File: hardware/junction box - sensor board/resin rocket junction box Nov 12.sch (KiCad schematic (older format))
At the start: 34 parts, among them P1 M3021-000005-2K5PG, P2 M3021-000005-2K5PG, T1 MCP9600, T2 MCP9600

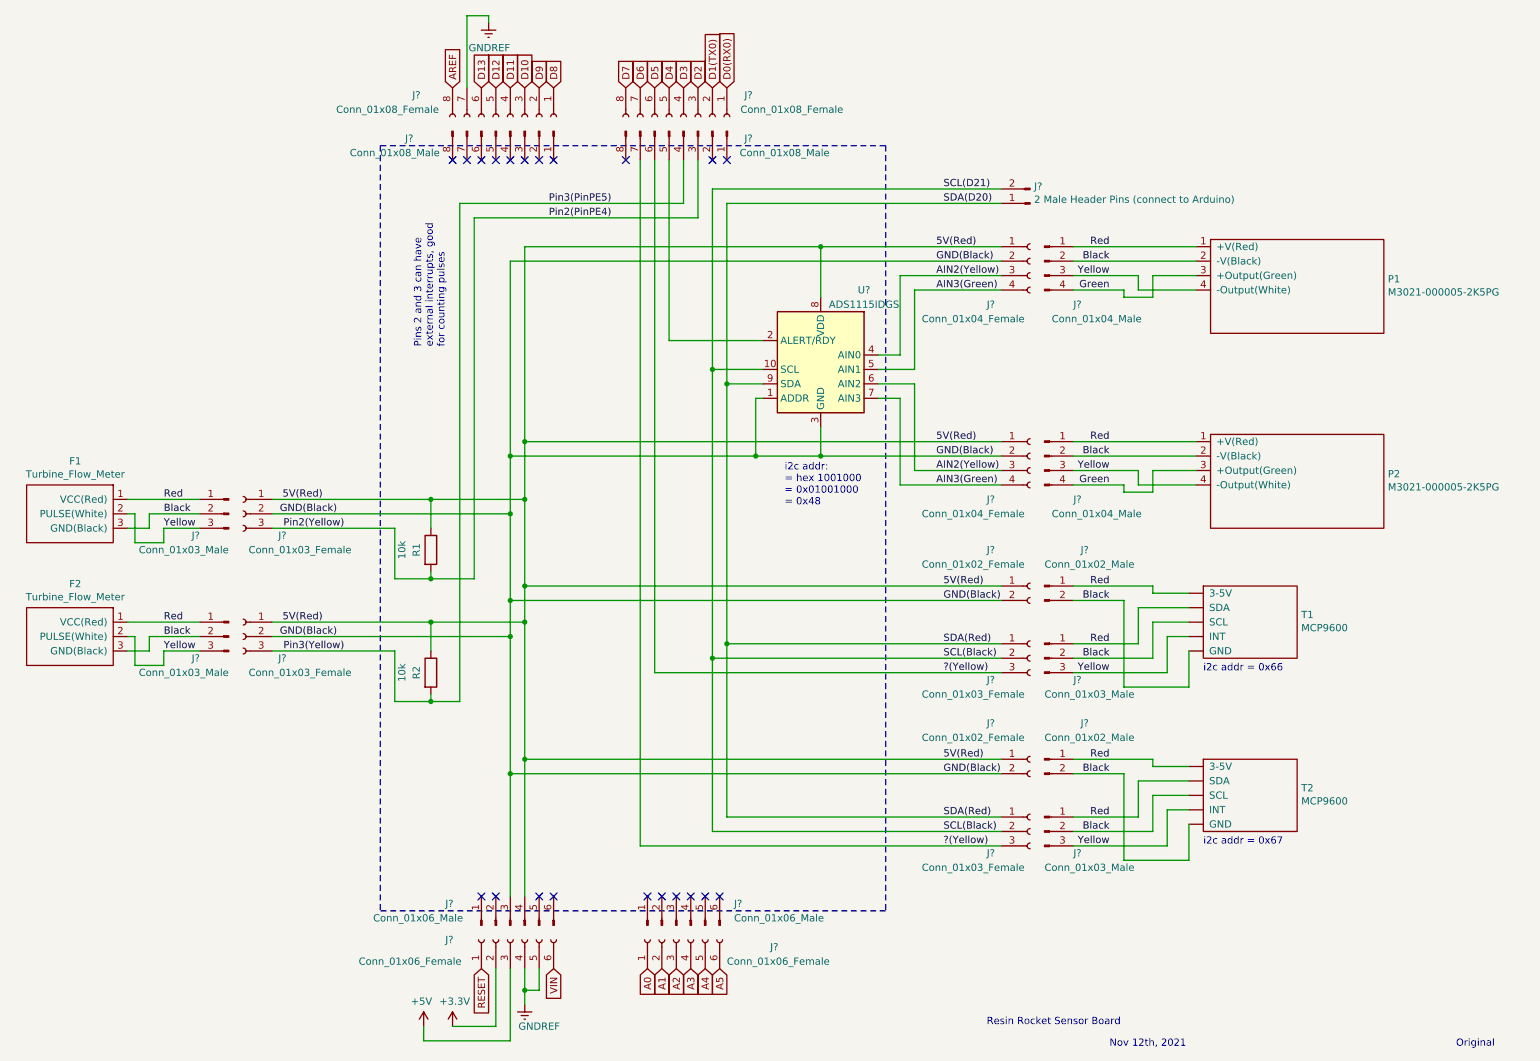
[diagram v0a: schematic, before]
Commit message: Updated all 3 schematics on Nov. 13th, 2021
Ground Station now includes buzzer, yellow LED, and voltage sensing circuit, to activate when key switch turns on high voltage lines (24V).

Split junction box boards into sensor board (connections to all sensors, ADCs, etc.) and high power board (controls the solenoids and igniter using 24V).
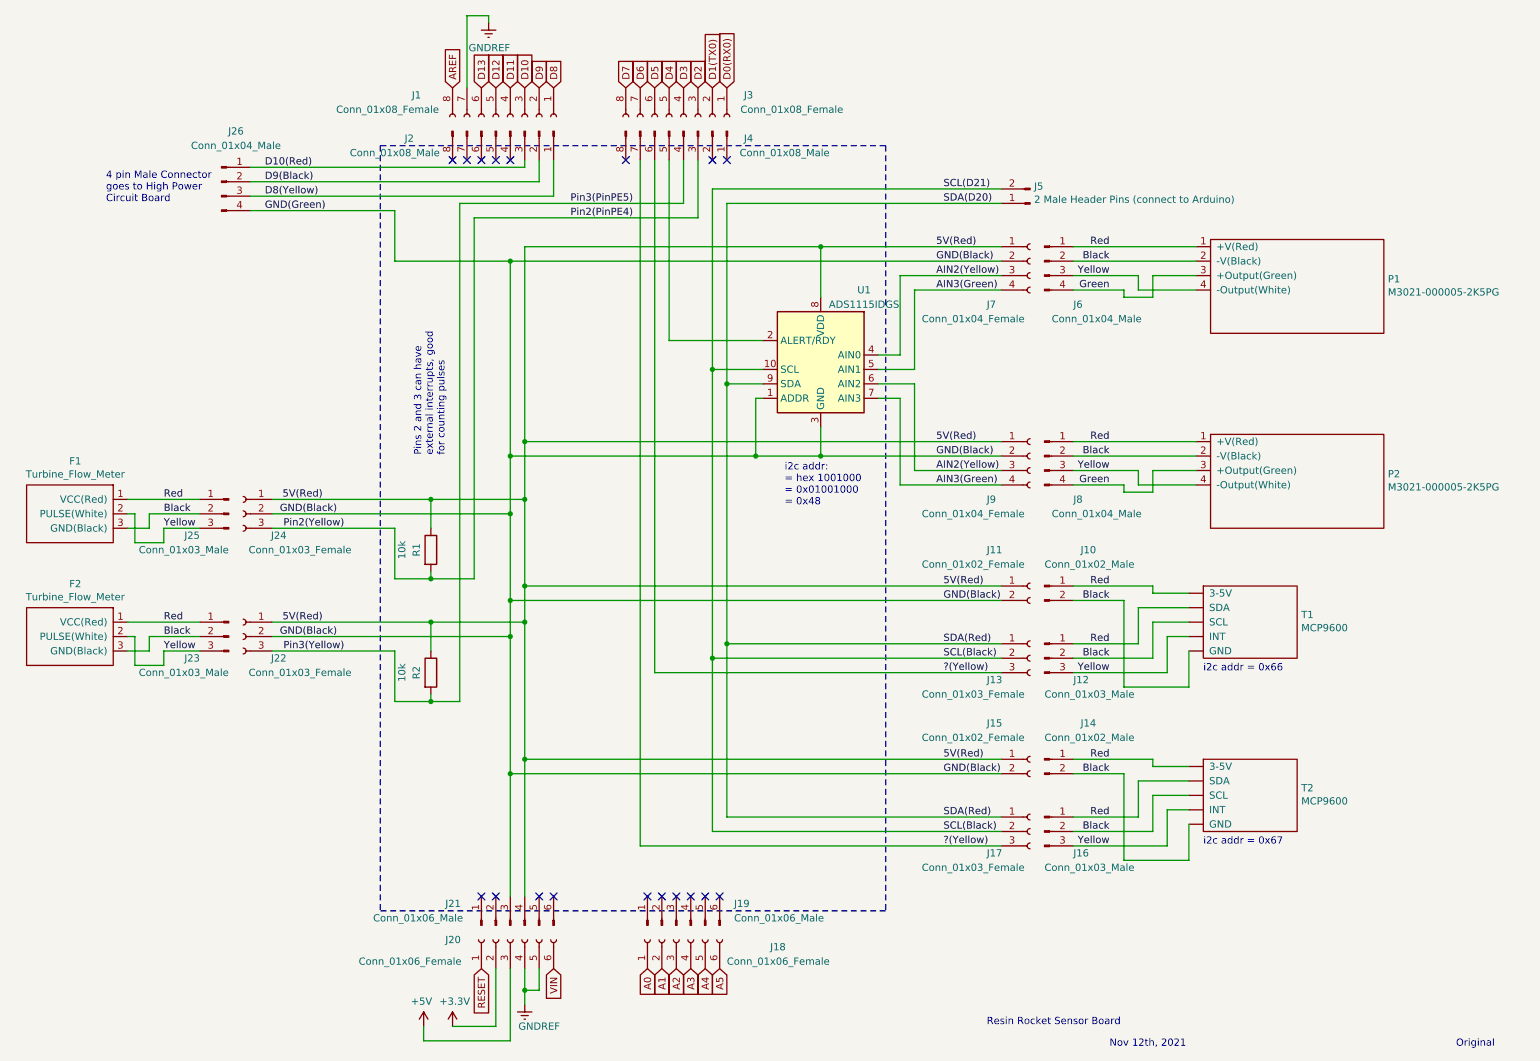
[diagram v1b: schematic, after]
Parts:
- added J26: Conn_01x04_Male, symbol Connector:Conn_01x04_Male
- gave numbers to parts that had none: 26
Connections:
- net GND(Black): now also J26.4 (Pin_4)
- net D8(Yellow): now reaches J2.1 (Pin_1)
- net D8(Yellow): now also J26.3 (Pin_3)
- net D9(Black): now reaches J2.2 (Pin_2)
- net D9(Black): now also J26.2 (Pin_2)
- net D10(Red): now reaches J2.3 (Pin_3)
- net D10(Red): now also J26.1 (Pin_1)
- no-connect marks 21 -> 18
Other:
- note added: "4 pin Male Connector\ngoes to High Power\nCircuit Board"
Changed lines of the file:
@@
 ?(Yellow)
 $Comp
-L Connector:Conn_01x02_Female J?
+L Connector:Conn_01x02_Female J11
 U 1 1 61A4BA22
 P 7650 4450
-F 0 "J?" H 7350 4700 50  0000 L CNN
+F 0 "J11" H 7350 4700 50  0000 L CNN
 F 1 "Conn_01x02_Female" H 6900 4600 50  0000 L CNN
 F 2 "" H 7650 4450 50  0001 C CNN
@@
 GND(Black)
 $Comp
-L Connector:Conn_01x08_Male J?
+L Connector:Conn_01x08_Male J4
 U 1 1 61A54FC3
 P 5250 1300
-F 0 "J?" V 5300 1750 50  0000 C CNN
+F 0 "J4" V 5300 1750 50  0000 C CNN
 F 1 "Conn_01x08_Male" V 5400 2000 50  0000 C CNN
 F 2 "" H 5250 1300 50  0001 C CNN
@@
 $EndComp
 $Comp
-L Connector:Conn_01x06_Male J?
+L Connector:Conn_01x06_Male J19
 U 1 1 61A572F0
 P 5200 6800
-F 0 "J?" V 5350 6400 50  0000 R CNN
+F 0 "J19" V 5350 6400 50  0000 R CNN
 F 1 "Conn_01x06_Male" V 5250 6400 50  0000 R CNN
 F 2 "" H 5200 6800 50  0001 C CNN
@@
 $EndComp
 $Comp
-L Connector:Conn_01x06_Male J?
+L Connector:Conn_01x06_Male J21
 U 1 1 61A58D90
 P 4050 6800
-F 0 "J?" V 4200 7250 50  0000 R CNN
+F 0 "J21" V 4200 7250 50  0000 R CNN
 F 1 "Conn_01x06_Male" V 4100 7750 50  0000 R CNN
 F 2 "" H 4050 6800 50  0001 C CNN
@@
 $EndComp
 $Comp
-L Connector:Conn_01x08_Male J?
+L Connector:Conn_01x08_Male J2
 U 1 1 61A5C83D
 P 4050 1300
-F 0 "J?" V 4100 600 50  0000 C CNN
+F 0 "J2" V 4100 600 50  0000 C CNN
 F 1 "Conn_01x08_Male" V 4200 500 50  0000 C CNN
 F 2 "" H 4050 1300 50  0001 C CNN
@@
 $EndComp
 $Comp
-L Connector:Conn_01x08_Female J?
+L Connector:Conn_01x08_Female J1
 U 1 1 61A6B10B
 P 4050 1200
-F 0 "J?" V 3900 550 50  0000 C CNN
+F 0 "J1" V 3900 550 50  0000 C CNN
 F 1 "Conn_01x08_Female" V 4000 350 50  0000 C CNN
 F 2 "" H 4050 1200 50  0001 C CNN
@@
 $EndComp
 $Comp
-L Connector:Conn_01x08_Female J?
+L Connector:Conn_01x08_Female J3
 U 1 1 61A6C27C
 P 5250 1200
-F 0 "J?" V 5100 1650 50  0000 C CNN
+F 0 "J3" V 5100 1650 50  0000 C CNN
 F 1 "Conn_01x08_Female" V 5200 1950 50  0000 C CNN
 F 2 "" H 5250 1200 50  0001 C CNN
@@
 $EndComp
 $Comp
-L Connector:Conn_01x06_Female J?
+L Connector:Conn_01x06_Female J18
 U 1 1 61A6DCB8
 P 5200 6900
-F 0 "J?" V 5150 6250 50  0000 R CNN
+F 0 "J18" V 5150 6250 50  0000 R CNN
 F 1 "Conn_01x06_Female" V 5050 6550 50  0000 R CNN
 F 2 "" H 5200 6900 50  0001 C CNN
@@
 $EndComp
 $Comp
-L Connector:Conn_01x06_Female J?
+L Connector:Conn_01x06_Female J20
 U 1 1 61A708D4
 P 4050 6900
-F 0 "J?" V 4050 7350 50  0000 R CNN
+F 0 "J20" V 4050 7350 50  0000 R CNN
 F 1 "Conn_01x06_Female" V 3900 7950 50  0000 R CNN
 F 2 "" H 4050 6900 50  0001 C CNN
@@
 Connection ~ 4150 7250
 $Comp
-L Analog_ADC:ADS1115IDGS U?
+L Analog_ADC:ADS1115IDGS U1
 U 1 1 61A37058
 P 6200 2950
-F 0 "U?" H 5900 3500 50  0000 C CNN
+F 0 "U1" H 5900 3500 50  0000 C CNN
 F 1 "ADS1115IDGS" H 5900 3400 50  0000 C CNN
 F 2 "Package_SO:TSSOP-10_3x3mm_P0.5mm" H 6200 2450 50  0001 C CNN
@@
 $EndComp
 $Comp
-L Connector:Conn_01x04_Female J?
+L Connector:Conn_01x04_Female J9
 U 1 1 61A97ECB
 P 7650 3550
-F 0 "J?" H 7350 3250 50  0000 L CNN
+F 0 "J9" H 7350 3250 50  0000 L CNN
 F 1 "Conn_01x04_Female" H 6900 3150 50  0000 L CNN
 F 2 "" H 7650 3550 50  0001 C CNN
@@
 AIN3(Green)
 $Comp
-L Connector:Conn_01x04_Male J?
+L Connector:Conn_01x04_Male J8
 U 1 1 61A9948C
 P 7750 3550
-F 0 "J?" H 7950 3250 50  0000 L CNN
+F 0 "J8" H 7950 3250 50  0000 L CNN
 F 1 "Conn_01x04_Male" H 7800 3150 50  0000 L CNN
 F 2 "" H 7750 3550 50  0001 C CNN
@@
 	6750 2850 6600 2850
 $Comp
-L Connector:Conn_01x03_Female J?
+L Connector:Conn_01x03_Female J13
 U 1 1 61A4BA16
 P 7650 4950
-F 0 "J?" H 7350 4800 50  0000 L CNN
+F 0 "J13" H 7350 4800 50  0000 L CNN
 F 1 "Conn_01x03_Female" H 6900 4700 50  0000 L CNN
 F 2 "" H 7650 4950 50  0001 C CNN
@@
 Yellow
 $Comp
-L Connector:Conn_01x02_Male J?
+L Connector:Conn_01x02_Male J10
 U 1 1 61AB93EA
 P 7750 4450
-F 0 "J?" H 8000 4700 50  0000 L CNN
+F 0 "J10" H 8000 4700 50  0000 L CNN
 F 1 "Conn_01x02_Male" H 7750 4600 50  0000 L CNN
 F 2 "" H 7750 4450 50  0001 C CNN
@@
 Black
 $Comp
-L Connector:Conn_01x03_Male J?
+L Connector:Conn_01x03_Male J12
 U 1 1 61AB93F4
 P 7750 4950
-F 0 "J?" H 7950 4800 50  0000 L CNN
+F 0 "J12" H 7950 4800 50  0000 L CNN
 F 1 "Conn_01x03_Male" H 7750 4700 50  0000 L CNN
 F 2 "" H 7750 4950 50  0001 C CNN
@@
 ?(Yellow)
 $Comp
-L Connector:Conn_01x02_Female J?
+L Connector:Conn_01x02_Female J15
 U 1 1 61AF18AA
 P 7650 5650
-F 0 "J?" H 7350 5900 50  0000 L CNN
+F 0 "J15" H 7350 5900 50  0000 L CNN
 F 1 "Conn_01x02_Female" H 6900 5800 50  0000 L CNN
 F 2 "" H 7650 5650 50  0001 C CNN
@@
 GND(Black)
 $Comp
-L Connector:Conn_01x03_Female J?
+L Connector:Conn_01x03_Female J17
 U 1 1 61AF18B2
 P 7650 6150
-F 0 "J?" H 7350 6000 50  0000 L CNN
+F 0 "J17" H 7350 6000 50  0000 L CNN
 F 1 "Conn_01x03_Female" H 6900 5900 50  0000 L CNN
 F 2 "" H 7650 6150 50  0001 C CNN
@@
 Yellow
 $Comp
-L Connector:Conn_01x02_Male J?
+L Connector:Conn_01x02_Male J14
 U 1 1 61AF18BB
 P 7750 5650
-F 0 "J?" H 8000 5900 50  0000 L CNN
+F 0 "J14" H 8000 5900 50  0000 L CNN
 F 1 "Conn_01x02_Male" H 7750 5800 50  0000 L CNN
 F 2 "" H 7750 5650 50  0001 C CNN
@@
 Black
 $Comp
-L Connector:Conn_01x03_Male J?
+L Connector:Conn_01x03_Male J16
 U 1 1 61AF18C3
 P 7750 6150
-F 0 "J?" H 7950 6000 50  0000 L CNN
+F 0 "J16" H 7950 6000 50  0000 L CNN
 F 1 "Conn_01x03_Male" H 7750 5900 50  0000 L CNN
 F 2 "" H 7750 6150 50  0001 C CNN
@@
 $EndComp
 $Comp
-L Connector:Conn_01x03_Male J?
+L Connector:Conn_01x03_Male J25
 U 1 1 61BDCDA4
 P 2100 3950
-F 0 "J?" H 2300 3800 50  0000 L CNN
+F 0 "J25" H 2300 3800 50  0000 L CNN
 F 1 "Conn_01x03_Male" H 2100 3700 50  0000 L CNN
 F 2 "" H 2100 3950 50  0001 C CNN
@@
 Yellow
 $Comp
-L Connector:Conn_01x03_Female J?
+L Connector:Conn_01x03_Female J24
 U 1 1 61BE319B
 P 2200 3950
-F 0 "J?" H 1900 3800 50  0000 L CNN
+F 0 "J24" H 1900 3800 50  0000 L CNN
 F 1 "Conn_01x03_Female" H 1450 3700 50  0000 L CNN
 F 2 "" H 2200 3950 50  0001 C CNN
@@
 $EndComp
 $Comp
-L Connector:Conn_01x03_Male J?
+L Connector:Conn_01x03_Male J23
 U 1 1 61C28E31
 P 2100 4800
-F 0 "J?" H 2300 4650 50  0000 L CNN
+F 0 "J23" H 2300 4650 50  0000 L CNN
 F 1 "Conn_01x03_Male" H 2100 4550 50  0000 L CNN
 F 2 "" H 2100 4800 50  0001 C CNN
@@
 Yellow
 $Comp
-L Connector:Conn_01x03_Female J?
+L Connector:Conn_01x03_Female J22
 U 1 1 61C28E3A
 P 2200 4800
-F 0 "J?" H 1900 4650 50  0000 L CNN
+F 0 "J22" H 1900 4650 50  0000 L CNN
 F 1 "Conn_01x03_Female" H 1450 4550 50  0000 L CNN
 F 2 "" H 2200 4800 50  0001 C CNN
@@
 GND(Black)
 $Comp
-L Connector:Conn_01x04_Female J?
+L Connector:Conn_01x04_Female J7
 U 1 1 61B0808F
 P 7650 2200
-F 0 "J?" H 7350 1900 50  0000 L CNN
+F 0 "J7" H 7350 1900 50  0000 L CNN
 F 1 "Conn_01x04_Female" H 6900 1800 50  0000 L CNN
 F 2 "" H 7650 2200 50  0001 C CNN
@@
 $EndComp
 $Comp
-L Connector:Conn_01x02_Male J?
+L Connector:Conn_01x02_Male J5
 U 1 1 61B036AF
 P 7650 1800
-F 0 "J?" H 7622 1682 50  0000 R CNN
+F 0 "J5" H 7622 1682 50  0000 R CNN
 F 1 "2 Male Header Pins (connect to Arduino)" H 7622 1773 50  0000 R CNN
 F 2 "" H 7650 1800 50  0001 C CNN
@@
 Red
 $Comp
-L Connector:Conn_01x04_Male J?
+L Connector:Conn_01x04_Male J6
 U 1 1 61AA8CA1
 P 7750 2200
-F 0 "J?" H 7950 1900 50  0000 L CNN
+F 0 "J6" H 7950 1900 50  0000 L CNN
 F 1 "Conn_01x04_Male" H 7800 1800 50  0000 L CNN
 F 2 "" H 7750 2200 50  0001 C CNN
@@
 Wire Wire Line
 	5250 1800 5250 1500
-Text Label 4750 1800 2    50   ~ 0
+Text Label 4900 1800 2    50   ~ 0
 Pin3(PinPE5)
 Wire Wire Line
@@
 Wire Wire Line
 	5350 1900 5350 1500
-Text Label 4750 1900 2    50   ~ 0
+Text Label 4900 1900 2    50   ~ 0
 Pin2(PinPE4)
 Wire Wire Line
 	3800 4400 3500 4400
 Connection ~ 3500 4400
-Text Notes 3600 2800 1    50   ~ 0
+Text Notes 3600 3550 1    50   ~ 0
 Pins 2 and 3 can have\nexternal interrupts, good \nfor counting pulses
 Wire Wire Line
@@
 NoConn ~ 3850 1500
 NoConn ~ 3950 1500
-NoConn ~ 4050 1500
-NoConn ~ 4150 1500
-NoConn ~ 4250 1500
-NoConn ~ 4350 1500
 Text GLabel 5450 1000 1    50   Input ~ 0
 D1(TX0)
@@
 Text Notes 10600 7650 0    50   ~ 0
 Original
+NoConn ~ 4050 1500
+Wire Wire Line
+	4150 1500 4150 1550
+Wire Wire Line
+	4150 1550 2250 1550
+Wire Wire Line
+	4250 1500 4250 1650
+Wire Wire Line
+	4250 1650 2250 1650
+Wire Wire Line
+	2250 1750 4350 1750
+Wire Wire Line
+	4350 1750 4350 1500
+$Comp
+L Connector:Conn_01x04_Male J26
+U 1 1 618FCEC3
+P 2050 1650
+F 0 "J26" H 2150 2000 50  0000 C CNN
+F 1 "Conn_01x04_Male" H 2150 1900 50  0000 C CNN
+F 2 "" H 2050 1650 50  0001 C CNN
+F 3 "~" H 2050 1650 50  0001 C CNN
+	1    2050 1650
+	1    0    0    -1
+$EndComp
+Wire Wire Line
+	4050 2200 3250 2200
+Wire Wire Line
+	3250 2200 3250 1850
+Wire Wire Line
+	3250 1850 2250 1850
+Connection ~ 4050 2200
+Text Label 2350 1550 0    50   ~ 0
+D10(Red)
+Text Label 2350 1650 0    50   ~ 0
+D9(Black)
+Text Label 2350 1750 0    50   ~ 0
+D8(Yellow)
+Text Label 2350 1850 0    50   ~ 0
+GND(Green)
+Text Notes 1250 1800 0    50   ~ 0
+4 pin Male Connector\ngoes to High Power\nCircuit Board
 $EndSCHEMATC
